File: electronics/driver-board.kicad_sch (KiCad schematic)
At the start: 65 parts, among them J1 Conn_01x02, J3 Motor_Conn_01x04, J5 Conn_01x06_Female, SW1 SW_Push, SW2 SW_Push, U2 LMR16020PDDAR, U3 ESP32-C6-MINI-1/U, U4 AMS1117-3.3, U5 TMC5240-TSSOP38, U6 MT6835, U7 AS5047D

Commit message: work on kibot
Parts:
- C1, C10, C16, C17, C19, C2, C20, C21, C26, C27, C28, C29, C3, C30, C31, C4, C5, C6, C7, C9, R1, R10, R11, R2, R3, R4, R7, R9: Package (none) -> 0603
- U2: Package (none) -> SOIC8
- U4: Package (none) -> SOT223-3
- U5: lcsc_part_number (none) -> SOP38-1EP
- U7: Package (none) -> SOP14
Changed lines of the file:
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@@
+      (effects (font (size 1.27 1.27)) hide)
+    )
+    (property "Package" "0603" (at 233.68 96.52 0)
       (effects (font (size 1.27 1.27)) hide)
     )
@@
     )
     (property "mfr_part_number" "CL10A226MO7JZNC" (at 140.335 49.53 0)
+      (effects (font (size 1.27 1.27)) hide)
+    )
+    (property "Package" "0603" (at 140.335 49.53 0)
       (effects (font (size 1.27 1.27)) hide)
     )
@@
     )
     (property "mfr_part_number" "LMR16020PDDAR" (at 96.52 47.625 0)
+      (effects (font (size 1.27 1.27)) hide)
+    )
+    (property "Package" "SOIC8" (at 96.52 47.625 0)
       (effects (font (size 1.27 1.27)) hide)
     )
@@
       (effects (font (size 1.27 1.27)) hide)
     )
+    (property "Package" "0603" (at 123.825 56.515 0)
+      (effects (font (size 1.27 1.27)) hide)
+    )
     (pin "1")
     (pin "2")
@@
       (effects (font (size 1.27 1.27)) hide)
     )
+    (property "Package" "0603" (at 313.69 49.53 0)
+      (effects (font (size 1.27 1.27)) hide)
+    )
     (pin "1")
     (pin "2")
@@
       (effects (font (size 1.27 1.27)) hide)
     )
+    (property "Package" "0603" (at 69.723 50.165 0)
+      (effects (font (size 1.27 1.27)) hide)
+    )
     (pin "1")
     (pin "2")
@@
     )
     (property "lcsc_part_number" "C23630" (at 52.07 178.435 0)
+      (effects (font (size 1.27 1.27)) hide)
+    )
+    (property "Package" "0603" (at 52.07 178.435 0)
       (effects (font (size 1.27 1.27)) hide)
     )
@@
     )
     (property "mfr_part_number" "AS5047P-ATSM" (at 195.58 159.385 0)
+      (effects (font (size 1.27 1.27)) hide)
+    )
+    (property "Package" "SOP14" (at 195.58 159.385 0)
       (effects (font (size 1.27 1.27)) hide)
     )
@@
       (effects (font (size 1.27 1.27)) hide)
     )
+    (property "Package" "0603" (at 177.8 49.53 0)
+      (effects (font (size 1.27 1.27)) hide)
+    )
     (pin "1")
     (pin "2")
@@
       (effects (font (size 1.27 1.27)) hide)
     )
+    (property "Package" "0603" (at 171.704 49.53 0)
+      (effects (font (size 1.27 1.27)) hide)
+    )
     (pin "1")
     (pin "2")
@@
       (effects (font (size 1.27 1.27)) hide)
     )
+    (property "Package" "0603" (at 85.725 33.655 90)
+      (effects (font (size 1.27 1.27)) hide)
+    )
     (pin "1")
     (pin "2")
@@
       (effects (font (size 1.27 1.27)) hide)
     )
+    (property "Package" "0603" (at 40.64 159.385 90)
+      (effects (font (size 1.27 1.27)) hide)
+    )
     (pin "1")
     (pin "2")
@@
       (effects (font (size 1.27 1.27)) hide)
     )
+    (property "Package" "0603" (at 273.05 55.88 0)
+      (effects (font (size 1.27 1.27)) hide)
+    )
     (pin "1")
     (pin "2")
@@
       (effects (font (size 1.27 1.27)) hide)
     )
+    (property "Package" "0603" (at 36.195 178.435 0)
+      (effects (font (size 1.27 1.27)) hide)
+    )
     (pin "1")
     (pin "2")
@@
       (effects (font (size 1.27 1.27)) hide)
     )
+    (property "Package" "0603" (at 134.62 167.005 90)
+      (effects (font (size 1.27 1.27)) hide)
+    )
     (pin "1")
     (pin "2")
@@
     )
     (property "lcsc_part_number" "C913904" (at 62.738 50.165 0)
+      (effects (font (size 1.27 1.27)) hide)
+    )
+    (property "Package" "0603" (at 62.738 50.165 0)
       (effects (font (size 1.27 1.27)) hide)
     )
@@
     )
     (property "mfr_part_number" "RT0603FRE1310KL" (at 40.64 128.905 90)
+      (effects (font (size 1.27 1.27)) hide)
+    )
+    (property "Package" "0603" (at 40.64 128.905 90)
       (effects (font (size 1.27 1.27)) hide)
     )
@@
       (effects (font (size 1.27 1.27)) hide)
     )
+    (property "Package" "0603" (at 365.125 213.995 0)
+      (effects (font (size 1.27 1.27)) hide)
+    )
     (pin "1")
     (pin "2")
@@
       (effects (font (size 1.27 1.27)) hide)
     )
+    (property "Package" "0603" (at 209.55 49.53 0)
+      (effects (font (size 1.27 1.27)) hide)
+    )
     (pin "1")
     (pin "2")
@@
     )
     (property "mfr_part_number" "RT0603FRE07100KL" (at 123.825 48.895 0)
+      (effects (font (size 1.27 1.27)) hide)
+    )
+    (property "Package" "0603" (at 123.825 48.895 0)
       (effects (font (size 1.27 1.27)) hide)
     )
@@
     )
     (property "lcsc_part_number" "C1592" (at 264.668 64.77 90)
+      (effects (font (size 1.27 1.27)) hide)
+    )
+    (property "Package" "0603" (at 264.668 64.77 90)
       (effects (font (size 1.27 1.27)) hide)
     )
@@
       (effects (font (size 1.27 1.27)) hide)
     )
+    (property "Package" "0603" (at 134.62 49.53 0)
+      (effects (font (size 1.27 1.27)) hide)
+    )
     (pin "1")
     (pin "2")
@@
       (effects (font (size 1.27 1.27)) hide)
     )
+    (property "Package" "0603" (at 55.753 50.165 0)
+      (effects (font (size 1.27 1.27)) hide)
+    )
     (pin "1")
     (pin "2")
@@
     )
     (property "lcsc_part_number" "C66501" (at 318.77 49.53 0)
+      (effects (font (size 1.27 1.27)) hide)
+    )
+    (property "Package" "0603" (at 318.77 49.53 0)
       (effects (font (size 1.27 1.27)) hide)
     )
@@
     )
     (property "mfr_part_number" "AMS1117-3.3" (at 191.77 42.545 0)
+      (effects (font (size 1.27 1.27)) hide)
+    )
+    (property "Package" "SOT223-3" (at 191.77 42.545 0)
       (effects (font (size 1.27 1.27)) hide)
     )
@@
       (effects (font (size 1.27 1.27)) hide)
     )
-    (property "lcsc_part_number" "" (at 91.44 151.765 0)
+    (property "lcsc_part_number" "SOP38-1EP" (at 91.44 151.765 0)
       (effects (font (size 1.27 1.27)) hide)
     )
@@
       (effects (font (size 1.27 1.27)) hide)
     )
+    (property "Package" "0603" (at 76.835 56.515 0)
+      (effects (font (size 1.27 1.27)) hide)
+    )
     (pin "1")
     (pin "2")
@@
       (effects (font (size 1.27 1.27)) hide)
     )
+    (property "Package" "0603" (at 203.835 49.53 0)
+      (effects (font (size 1.27 1.27)) hide)
+    )
     (pin "1")
     (pin "2")
@@
       (effects (font (size 1.27 1.27)) hide)
     )
+    (property "Package" "0603" (at 308.61 49.53 0)
+      (effects (font (size 1.27 1.27)) hide)
+    )
     (pin "1")
     (pin "2")
@@
     )
     (property "lcsc_part_number" "C4226066" (at 276.86 55.88 0)
+      (effects (font (size 1.27 1.27)) hide)
+    )
+    (property "Package" "0603" (at 276.86 55.88 0)
       (effects (font (size 1.27 1.27)) hide)
     )
@@
       (effects (font (size 1.27 1.27)) hide)
     )
+    (property "Package" "0603" (at 212.09 172.72 0)
+      (effects (font (size 1.27 1.27)) hide)
+    )
     (pin "1")
     (pin "2")
@@
       (effects (font (size 1.27 1.27)) hide)
     )
+    (property "Package" "0603" (at 146.05 49.53 0)
+      (effects (font (size 1.27 1.27)) hide)
+    )

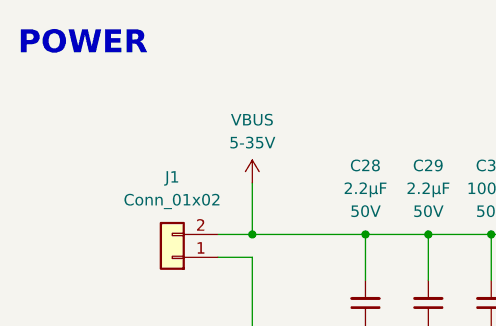
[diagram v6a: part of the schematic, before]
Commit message: renders without commit hash
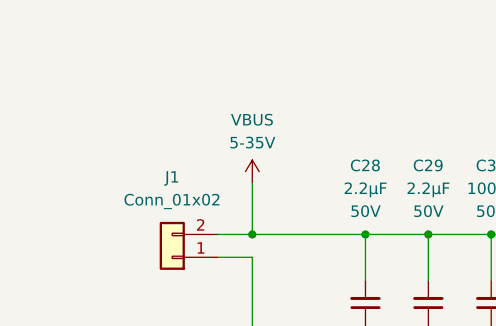
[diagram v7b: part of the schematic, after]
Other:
- note removed: "POWER"
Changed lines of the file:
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@@
     (effects (font (size 1 1)) (justify right bottom))
-  )
-  (text "POWER" (at 17.145 22.86 0)
-    (effects (font (size 2.54 2.54) (thickness 0.508) bold) (justify left bottom))
   )
   (label "TMC_ENCN" (at 137.795 156.845 180) (fields_autoplaced)
